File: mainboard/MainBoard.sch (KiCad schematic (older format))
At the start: 47 parts, among them J1 isoSPI, J2 SWDebug, J3 IMD, J4 IO, U1 LTC6820, U10 REF2920, U2 HM2103, U3 M24M02, U4 M24M02, U5 STM32F334K8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

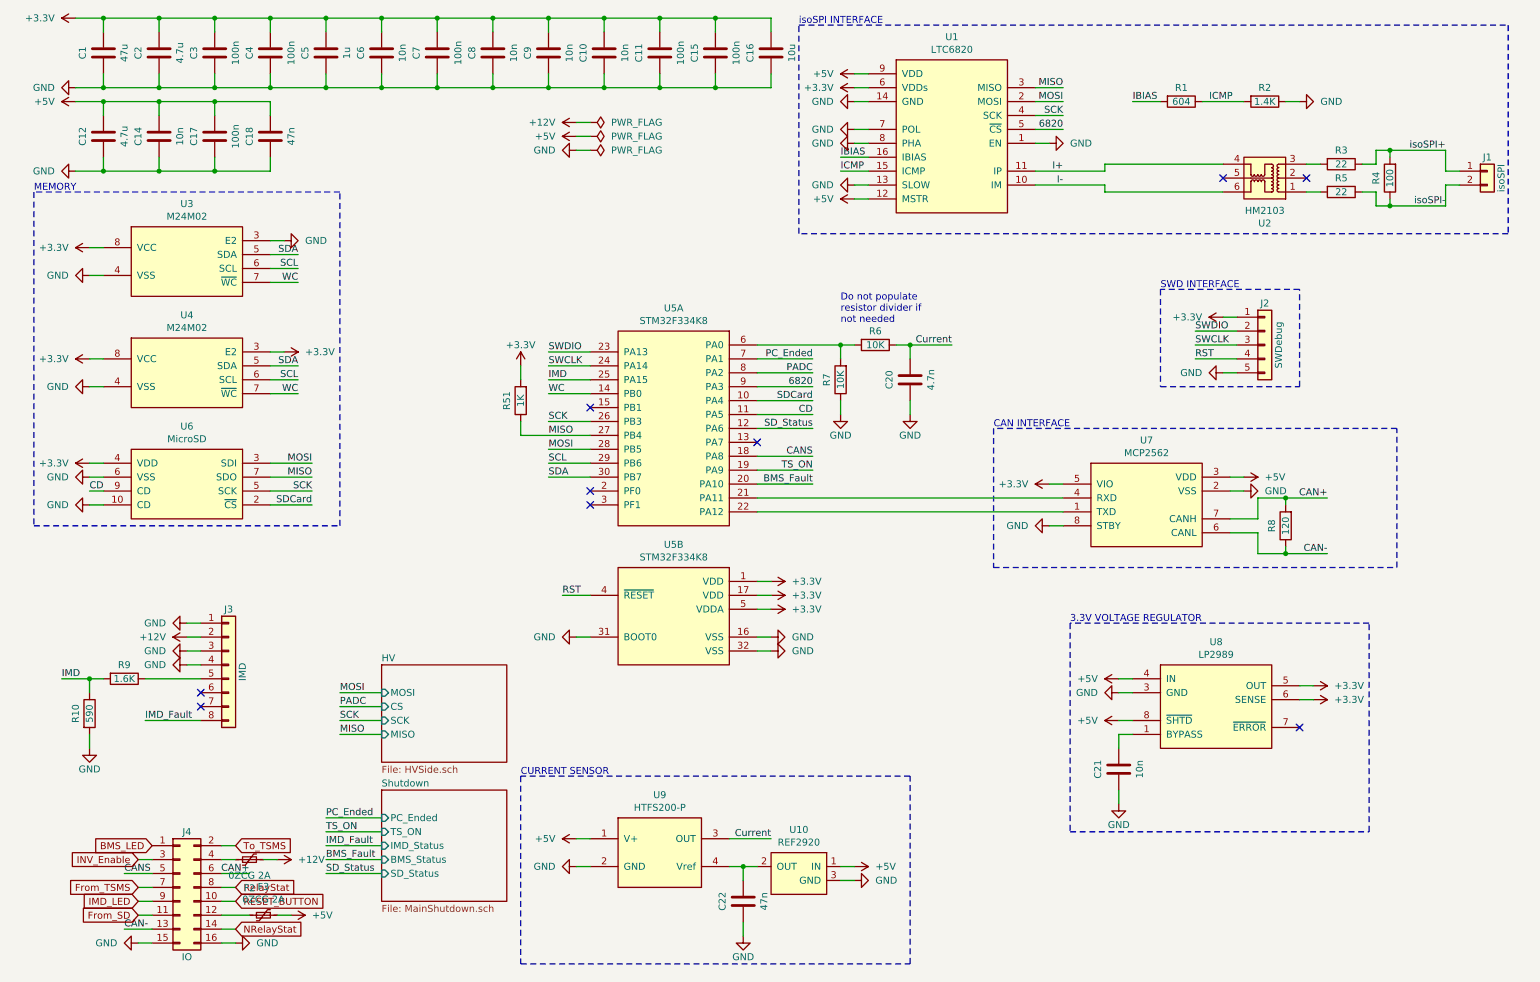
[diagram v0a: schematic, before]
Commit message: change isoadc in schematic and documents
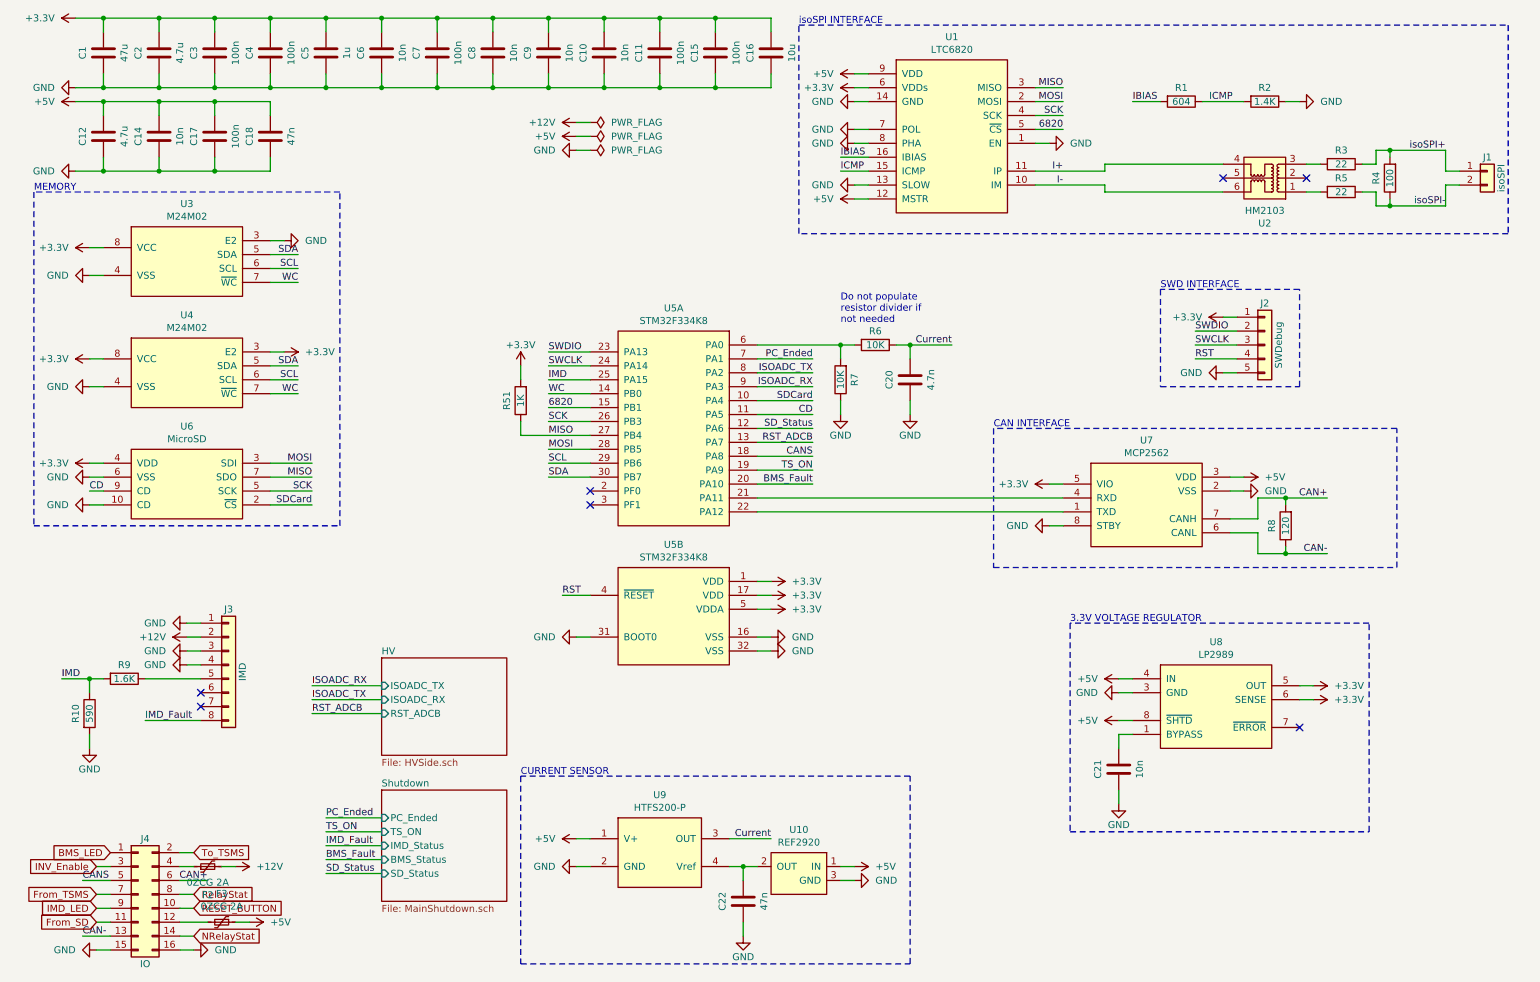
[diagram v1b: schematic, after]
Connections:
- net 6820: now also U5.15 (PB1); no longer U5.9 (PA3)
- net RST_ADCB: now reaches U5.13 (PA7)
- net PADC renamed ISOADC_TX
- new net ISOADC_RX: U5.9 (PA3)
- no-connect marks 9 -> 7
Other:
- moved on the sheet: F2, F3, J4
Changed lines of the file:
@@
 	0    -1   -1   0
 $EndComp
-Text GLabel 1450 6500 0    50   Input ~ 0
+Text GLabel 1150 6550 0    50   Input ~ 0
 BMS_LED
-Text GLabel 2050 6500 2    50   Input ~ 0
+Text GLabel 1750 6550 2    50   Input ~ 0
 To_TSMS
-Text GLabel 2050 6900 2    50   Input ~ 0
+Text GLabel 1750 6950 2    50   Input ~ 0
 RESET_BUTTON
-Text GLabel 1350 6800 0    50   Input ~ 0
+Text GLabel 1050 6850 0    50   Input ~ 0
 From_TSMS
 Wire Wire Line
@@
 Text Label 2700 6300 0    50   ~ 0
 PC_Ended
-Text Label 6200 3000 2    50   ~ 0
-PC_Ended
 Wire Wire Line
 	5800 3000 6200 3000
@@
 Text Label 800  5300 0    50   ~ 0
 IMD
-$Sheet
-S 3100 5200 900  700
-U 5B50ED38
-F0 "HV" 50
-F1 "HVSide.sch" 50
-F2 "MOSI" I L 3100 5400 50
-F3 "CS" I L 3100 5500 50
-F4 "SCK" I L 3100 5600 50
-F5 "MISO" I L 3100 5700 50
-$EndSheet
-Wire Wire Line
-	2800 5400 3100 5400
-Wire Wire Line
-	3100 5500 2800 5500
-Wire Wire Line
-	3100 5600 2800 5600
-Wire Wire Line
-	3100 5700 2800 5700
-Text Label 2800 5400 0    50   ~ 0
-MOSI
-Text Label 2800 5500 0    50   ~ 0
-PADC
-Text Label 2800 5600 0    50   ~ 0
-SCK
-Text Label 2800 5700 0    50   ~ 0
-MISO
-Text Label 6200 3100 2    50   ~ 0
-PADC
-Wire Wire Line
-	5800 3100 6200 3100
-NoConn ~ 4600 3350
 NoConn ~ 4600 3950
 NoConn ~ 4600 4050
-NoConn ~ 5800 3600
-Wire Wire Line
-	5800 3200 6200 3200
-Text Label 6200 3200 2    50   ~ 0
+Wire Wire Line
+	4600 3350 4300 3350
+Text Label 4300 3350 0    50   ~ 0
 6820
 Text Label 8000 1350 2    50   ~ 0
 6820
-Text GLabel 2050 6800 2    50   Input ~ 0
+Text GLabel 1750 6850 2    50   Input ~ 0
 RelayStat
-Text GLabel 2050 7100 2    50   Input ~ 0
+Text GLabel 1750 7150 2    50   Input ~ 0
 NRelayStat
 $Comp
@@
 $EndComp
 Wire Wire Line
-	1950 6600 2050 6600
+	1650 6650 1750 6650
 $Comp
 L power:+12V #PWR053
 U 1 1 5BA2D579
-P 2350 6600
-F 0 "#PWR053" H 2350 6450 50  0001 C CNN
-F 1 "+12V" V 2350 6750 50  0000 L CNN
-F 2 "" H 2350 6600 50  0001 C CNN
-F 3 "" H 2350 6600 50  0001 C CNN
-	1    2350 6600
+P 2050 6650
+F 0 "#PWR053" H 2050 6500 50  0001 C CNN
+F 1 "+12V" V 2050 6800 50  0000 L CNN
+F 2 "" H 2050 6650 50  0001 C CNN
+F 3 "" H 2050 6650 50  0001 C CNN
+	1    2050 6650
 	0    1    1    0
 $EndComp
@@
 L power:+5V #PWR054
 U 1 1 5BA3CD38
-P 2450 7000
-F 0 "#PWR054" H 2450 6850 50  0001 C CNN
-F 1 "+5V" V 2450 7150 50  0000 L CNN
-F 2 "" H 2450 7000 50  0001 C CNN
-F 3 "" H 2450 7000 50  0001 C CNN
-	1    2450 7000
-	0    1    1    0
-$EndComp
-Wire Wire Line
-	2150 6700 1950 6700
-Text Label 2150 6700 2    50   ~ 0
+P 2150 7050
+F 0 "#PWR054" H 2150 6900 50  0001 C CNN
+F 1 "+5V" V 2150 7200 50  0000 L CNN
+F 2 "" H 2150 7050 50  0001 C CNN
+F 3 "" H 2150 7050 50  0001 C CNN
+	1    2150 7050
+	0    1    1    0
+$EndComp
+Wire Wire Line
+	1850 6750 1650 6750
+Text Label 1850 6750 2    50   ~ 0
 CAN+
-Text Label 1250 7100 0    50   ~ 0
+Text Label 950  7150 0    50   ~ 0
 CAN-
 Wire Wire Line
-	1950 6500 2050 6500
-Text GLabel 1350 7000 0    50   Input ~ 0
+	1650 6550 1750 6550
+Text GLabel 1050 7050 0    50   Input ~ 0
 From_SD
 Wire Wire Line
-	1350 6800 1450 6800
-Wire Wire Line
-	1950 6800 2050 6800
-Wire Wire Line
-	1450 6900 1350 6900
-Text GLabel 1350 6600 0    50   Input ~ 0
+	1050 6850 1150 6850
+Wire Wire Line
+	1650 6850 1750 6850
+Wire Wire Line
+	1150 6950 1050 6950
+Text GLabel 1050 6650 0    50   Input ~ 0
 INV_Enable
 Wire Wire Line
-	1950 6900 2050 6900
-Wire Wire Line
-	1450 7000 1350 7000
-Text GLabel 1350 6900 0    50   Input ~ 0
+	1650 6950 1750 6950
+Wire Wire Line
+	1150 7050 1050 7050
+Text GLabel 1050 6950 0    50   Input ~ 0
 IMD_LED
 $Comp
 L Connector_Generic:Conn_02x08_Odd_Even J4
 U 1 1 5BBA5FCF
-P 1650 6800
-F 0 "J4" H 1700 7200 50  0000 C CNN
-F 1 "IO" H 1700 6300 50  0000 C CNN
-F 2 "Connector_Molex:Molex_Micro-Fit_3.0_43045-1612_2x08_P3.00mm_Vertical" H 1650 6800 50  0001 C CNN
-F 3 "~" H 1650 6800 50  0001 C CNN
-	1    1650 6800
+P 1350 6850
+F 0 "J4" H 1400 7250 50  0000 C CNN
+F 1 "IO" H 1400 6350 50  0000 C CNN
+F 2 "Connector_Molex:Molex_Micro-Fit_3.0_43045-1612_2x08_P3.00mm_Vertical" H 1350 6850 50  0001 C CNN
+F 3 "~" H 1350 6850 50  0001 C CNN
+	1    1350 6850
 	1    0    0    -1
 $EndComp
@@
 CANS
 Wire Wire Line
-	1450 6700 1250 6700
-Text Label 1250 6700 0    50   ~ 0
+	1150 6750 950  6750
+Text Label 950  6750 0    50   ~ 0
 CANS
 Wire Wire Line
-	1450 7200 1350 7200
-Wire Wire Line
-	1950 7200 2050 7200
+	1150 7250 1050 7250
+Wire Wire Line
+	1650 7250 1750 7250
 $Comp
 L power:GND #PWR059
 U 1 1 5BC6DC6E
-P 1350 7200
-F 0 "#PWR059" H 1350 6950 50  0001 C CNN
-F 1 "GND" V 1350 7050 50  0000 R CNN
-F 2 "" H 1350 7200 50  0001 C CNN
-F 3 "" H 1350 7200 50  0001 C CNN
-	1    1350 7200
+P 1050 7250
+F 0 "#PWR059" H 1050 7000 50  0001 C CNN
+F 1 "GND" V 1050 7100 50  0000 R CNN
+F 2 "" H 1050 7250 50  0001 C CNN
+F 3 "" H 1050 7250 50  0001 C CNN
+	1    1050 7250
 	0    1    1    0
 $EndComp
@@
 L power:GND #PWR060
 U 1 1 5BC6DE63
-P 2050 7200
-F 0 "#PWR060" H 2050 6950 50  0001 C CNN
-F 1 "GND" V 2050 7050 50  0000 R CNN
-F 2 "" H 2050 7200 50  0001 C CNN
-F 3 "" H 2050 7200 50  0001 C CNN
-	1    2050 7200
+P 1750 7250
+F 0 "#PWR060" H 1750 7000 50  0001 C CNN
+F 1 "GND" V 1750 7100 50  0000 R CNN
+F 2 "" H 1750 7250 50  0001 C CNN
+F 3 "" H 1750 7250 50  0001 C CNN
+	1    1750 7250
 	0    -1   -1   0
 $EndComp
@@
 U 1 1 5B1DCFF8
 P 6400 3150
-F 0 "R7" V 6500 3150 50  0000 C CNN
+F 0 "R7" V 6300 3150 50  0000 C CNN
 F 1 "10K" V 6400 3150 50  0000 C CNN
 F 2 "Resistor_SMD:R_0805_2012Metric" V 6330 3150 50  0001 C CNN
@@
 L Device:Polyfuse_Small F2
 U 1 1 5B2F3DA2
-P 2150 6600
-F 0 "F2" V 1945 6600 50  0000 C CNN
-F 1 "0ZCG 2A" V 2036 6600 50  0000 C CNN
-F 2 "Fuse:Fuse_1812_4532Metric" H 2200 6400 50  0001 L CNN
-F 3 "~" H 2150 6600 50  0001 C CNN
-	1    2150 6600
+P 1850 6650
+F 0 "F2" V 1645 6650 50  0000 C CNN
+F 1 "0ZCG 2A" V 1736 6650 50  0000 C CNN
+F 2 "Fuse:Fuse_1812_4532Metric" H 1900 6450 50  0001 L CNN
+F 3 "~" H 1850 6650 50  0001 C CNN
+	1    1850 6650
 	0    -1   -1   0
 $EndComp
 Wire Wire Line
-	2250 6600 2350 6600
+	1950 6650 2050 6650
 $Comp
 L Device:Polyfuse_Small F3
 U 1 1 5B3092A1
-P 2250 7000
-F 0 "F3" V 2045 7000 50  0000 C CNN
-F 1 "0ZCG 2A" V 2136 7000 50  0000 C CNN
-F 2 "Fuse:Fuse_1812_4532Metric" H 2300 6800 50  0001 L CNN
-F 3 "~" H 2250 7000 50  0001 C CNN
-	1    2250 7000
-	0    1    1    0
-$EndComp
-Wire Wire Line
-	2350 7000 2450 7000
-Wire Wire Line
-	1950 7000 2150 7000
-Wire Wire Line
-	1450 6600 1350 6600
-Wire Wire Line
-	1250 7100 1450 7100
-Wire Wire Line
-	1950 7100 2050 7100
+P 1950 7050
+F 0 "F3" V 1745 7050 50  0000 C CNN
+F 1 "0ZCG 2A" V 1836 7050 50  0000 C CNN
+F 2 "Fuse:Fuse_1812_4532Metric" H 2000 6850 50  0001 L CNN
+F 3 "~" H 1950 7050 50  0001 C CNN
+	1    1950 7050
+	0    1    1    0
+$EndComp
+Wire Wire Line
+	2050 7050 2150 7050
+Wire Wire Line
+	1650 7050 1850 7050
+Wire Wire Line
+	1150 6650 1050 6650
+Wire Wire Line
+	950  7150 1150 7150
+Wire Wire Line
+	1650 7150 1750 7150
+$Sheet
+S 3100 5150 900  700
+U 5B50ED38
+F0 "HV" 50
+F1 "HVSide.sch" 50
+F2 "ISOADC_TX" I L 3100 5350 50
+F3 "ISOADC_RX" I L 3100 5450 50
+F4 "RST_ADCB" I L 3100 5550 50
+$EndSheet
+Text Label 6200 3000 2    50   ~ 0
+PC_Ended
+Text Label 2600 5350 0    50   ~ 0
+ISOADC_RX
+Text Label 2600 5450 0    50   ~ 0
+ISOADC_TX
+Text Label 2600 5550 0    50   ~ 0
+RST_ADCB
+Wire Wire Line
+	2600 5350 3100 5350
+Wire Wire Line
+	2600 5450 3100 5450
+Wire Wire Line
+	3100 5550 2600 5550
+Text Label 6200 3200 2    50   ~ 0
+ISOADC_RX
+Text Label 6200 3100 2    50   ~ 0
+ISOADC_TX
+Wire Wire Line
+	6200 3200 5800 3200
+Wire Wire Line
+	6200 3100 5800 3100
+Wire Wire Line
+	5800 3600 6200 3600
+Text Label 6200 3600 2    50   ~ 0
+RST_ADCB
 $EndSCHEMATC

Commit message: i2c isoadc 8901
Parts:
- added R57, R58: 2k, Resistor_SMD:R_0805_2012Metric, symbol Device:R
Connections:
- net +3V3: now also R57.2, R58.2
- net SCL: now also R58.1
- net SDA: now also R57.1
- net ISOADC_RX: no longer names the net of U5.9 (PA3)
- net ISOADC_TX: no longer names the net of U5.8 (PA2)
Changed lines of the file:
@@
 SDA
-Wire Wire Line
-	4300 3750 4600 3750
-Wire Wire Line
-	4300 3850 4600 3850
 Wire Wire Line
 	2300 2250 2500 2250
@@
 $EndComp
 Wire Wire Line
-	4100 3150 4100 3050
+	4100 3150 4100 3100
 $Comp
 L power:+3.3V #PWR0141
@@
 F0 "HV" 50
 F1 "HVSide.sch" 50
-F2 "ISOADC_TX" I L 3100 5350 50
-F3 "ISOADC_RX" I L 3100 5450 50
-F4 "RST_ADCB" I L 3100 5550 50
+F2 "SDA" I L 3100 5300 50
+F3 "SCL" I L 3100 5400 50
+F4 "RST_ADCB" I L 3100 5500 50
 $EndSheet
 Text Label 6200 3000 2    50   ~ 0
 PC_Ended
-Text Label 2600 5350 0    50   ~ 0
-ISOADC_RX
-Text Label 2600 5450 0    50   ~ 0
-ISOADC_TX
-Text Label 2600 5550 0    50   ~ 0
-RST_ADCB
-Wire Wire Line
-	2600 5350 3100 5350
-Wire Wire Line
-	2600 5450 3100 5450
-Wire Wire Line
-	3100 5550 2600 5550
-Text Label 6200 3200 2    50   ~ 0
-ISOADC_RX
-Text Label 6200 3100 2    50   ~ 0
-ISOADC_TX
-Wire Wire Line
-	6200 3200 5800 3200
-Wire Wire Line
-	6200 3100 5800 3100
 Wire Wire Line
 	5800 3600 6200 3600
 Text Label 6200 3600 2    50   ~ 0
 RST_ADCB
+$Comp
+L Device:R R58
+U 1 1 603E2CED
+P 3900 3300
+F 0 "R58" V 4000 3300 50  0000 C CNN
+F 1 "2k" V 3900 3300 50  0000 C CNN
+F 2 "Resistor_SMD:R_0805_2012Metric" V 3830 3300 50  0001 C CNN
+F 3 "~" H 3900 3300 50  0001 C CNN
+	1    3900 3300
+	-1   0    0    1
+$EndComp
+$Comp
+L Device:R R57
+U 1 1 603E3010
+P 3700 3300
+F 0 "R57" V 3800 3300 50  0000 C CNN
+F 1 "2k" V 3700 3300 50  0000 C CNN
+F 2 "Resistor_SMD:R_0805_2012Metric" V 3630 3300 50  0001 C CNN
+F 3 "~" H 3700 3300 50  0001 C CNN
+	1    3700 3300
+	-1   0    0    1
+$EndComp
+Wire Wire Line
+	4100 3100 3900 3100
+Wire Wire Line
+	3700 3100 3700 3150
+Connection ~ 4100 3100
+Wire Wire Line
+	4100 3100 4100 3050
+Wire Wire Line
+	3900 3150 3900 3100
+Connection ~ 3900 3100
+Wire Wire Line
+	3900 3100 3700 3100
+Wire Wire Line
+	3900 3450 3900 3750
+Wire Wire Line
+	3900 3750 4600 3750
+Wire Wire Line
+	3700 3850 3700 3450
+Wire Wire Line
+	3700 3850 4600 3850
+Text Label 2700 5400 0    50   ~ 0
+SCL
+Text Label 2700 5300 0    50   ~ 0
+SDA
+Text Label 2700 5500 0    50   ~ 0
+RST_ADCB
+Wire Wire Line
+	2700 5300 3100 5300
+Wire Wire Line
+	3100 5400 2700 5400
+Wire Wire Line
+	3100 5500 2700 5500
 $EndSCHEMATC

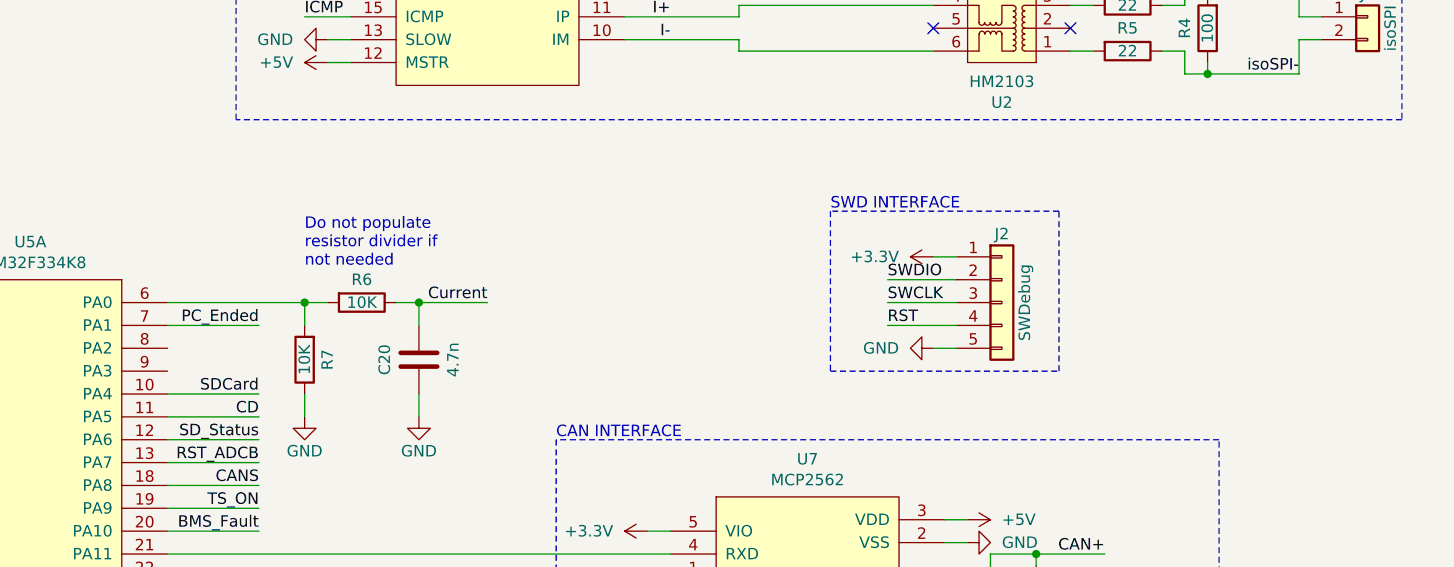
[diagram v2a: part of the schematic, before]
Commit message: adding handcart detection
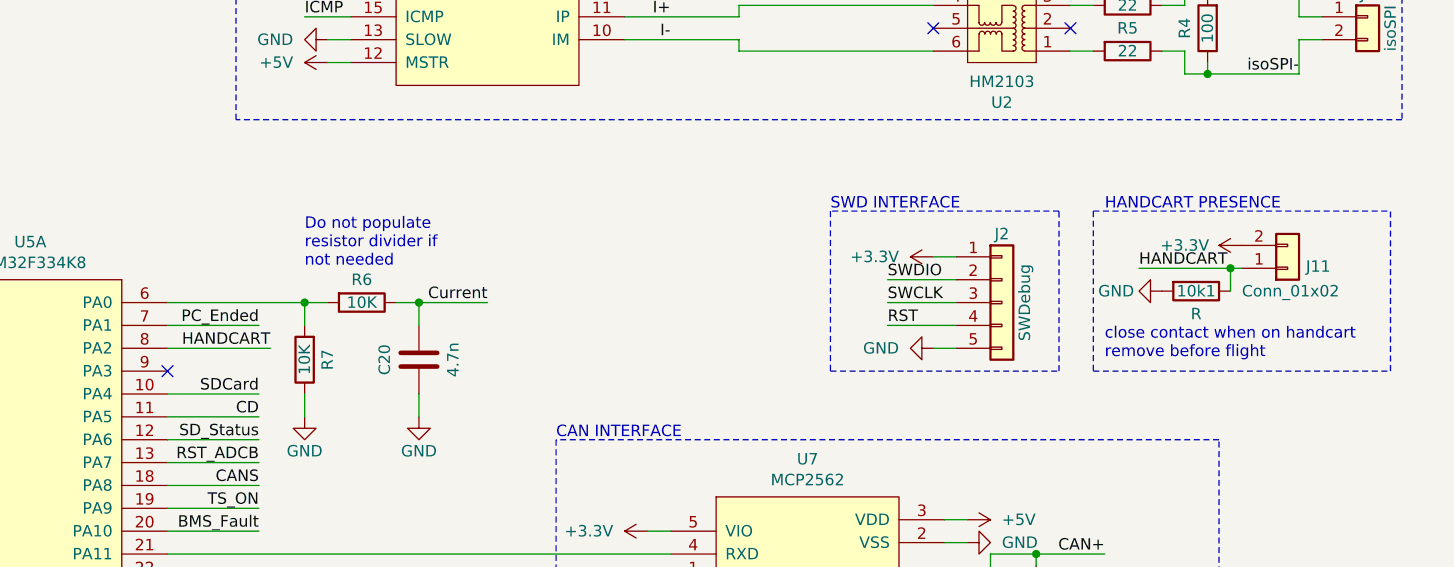
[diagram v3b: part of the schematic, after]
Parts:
- added 10k1: R, symbol Device:R
- added J11: Conn_01x02, symbol Connector_Generic:Conn_01x02
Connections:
- net +3V3: now also J11.2 (Pin_2)
- net GND: now also 10k1.2
- net HANDCART: now reaches U5.8 (PA2)
- net HANDCART: now also 10k1.1, J11.1 (Pin_1)
- no-connect marks 7 -> 8
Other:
- note added: "HANDCART PRESENCE"
- note added: "close contact when on handcart\nremove before flight"
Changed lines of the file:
@@
 Wire Wire Line
 	3100 5500 2700 5500
+Wire Wire Line
+	5800 3100 6250 3100
+Text Label 6250 3100 2    50   ~ 0
+HANDCART
+Text Label 10050 2750 0    50   ~ 0
+HANDCART
+$Comp
+L Device:R 10k1
+U 1 1 6050CC83
+P 10300 2850
+F 0 "10k1" V 10300 2850 50  0000 C CNN
+F 1 "R" V 10400 2850 50  0000 C CNN
+F 2 "" V 10230 2850 50  0001 C CNN
+F 3 "~" H 10300 2850 50  0001 C CNN
+	1    10300 2850
+	0    1    1    0
+$EndComp
+$Comp
+L Connector_Generic:Conn_01x02 J11
+U 1 1 605176BC
+P 10700 2750
+F 0 "J11" H 10780 2742 50  0000 L CNN
+F 1 "Conn_01x02" H 10500 2850 50  0000 L CNN
+F 2 "" H 10700 2750 50  0001 C CNN
+F 3 "~" H 10700 2750 50  0001 C CNN
+	1    10700 2750
+	1    0    0    1
+$EndComp
+Wire Wire Line
+	10050 2750 10450 2750
+$Comp
+L power:+3.3V #PWR0147
+U 1 1 6059CB2E
+P 10500 2650
+F 0 "#PWR0147" H 10500 2500 50  0001 C CNN
+F 1 "+3.3V" V 10500 2900 50  0000 C CNN
+F 2 "" H 10500 2650 50  0001 C CNN
+F 3 "" H 10500 2650 50  0001 C CNN
+	1    10500 2650
+	0    -1   1    0
+$EndComp
+$Comp
+L power:GND #PWR0146
+U 1 1 605F6B8B
+P 10150 2850
+F 0 "#PWR0146" H 10150 2600 50  0001 C CNN
+F 1 "GND" V 10150 2650 50  0000 C CNN
+F 2 "" H 10150 2850 50  0001 C CNN
+F 3 "" H 10150 2850 50  0001 C CNN
+	1    10150 2850
+	0    1    1    0
+$EndComp
+Wire Wire Line
+	10450 2850 10450 2750
+Connection ~ 10450 2750
+Wire Wire Line
+	10450 2750 10500 2750
+Text Notes 9900 2500 0    50   ~ 0
+HANDCART PRESENCE
+Text Notes 9900 3150 0    50   ~ 0
+close contact when on handcart\nremove before flight
+Wire Notes Line
+	9850 2500 9850 3200
+Wire Notes Line
+	11150 3200 11150 2500
+Wire Notes Line
+	9850 2500 11150 2500
+Wire Notes Line
+	9850 3200 11150 3200
+NoConn ~ 5800 3200
 $EndSCHEMATC
